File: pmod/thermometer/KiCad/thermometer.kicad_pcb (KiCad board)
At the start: 2 copper layers, 23 x 17 mm, 4 parts, among them J1 Conn_01x06_Pin, U1 DS18B20

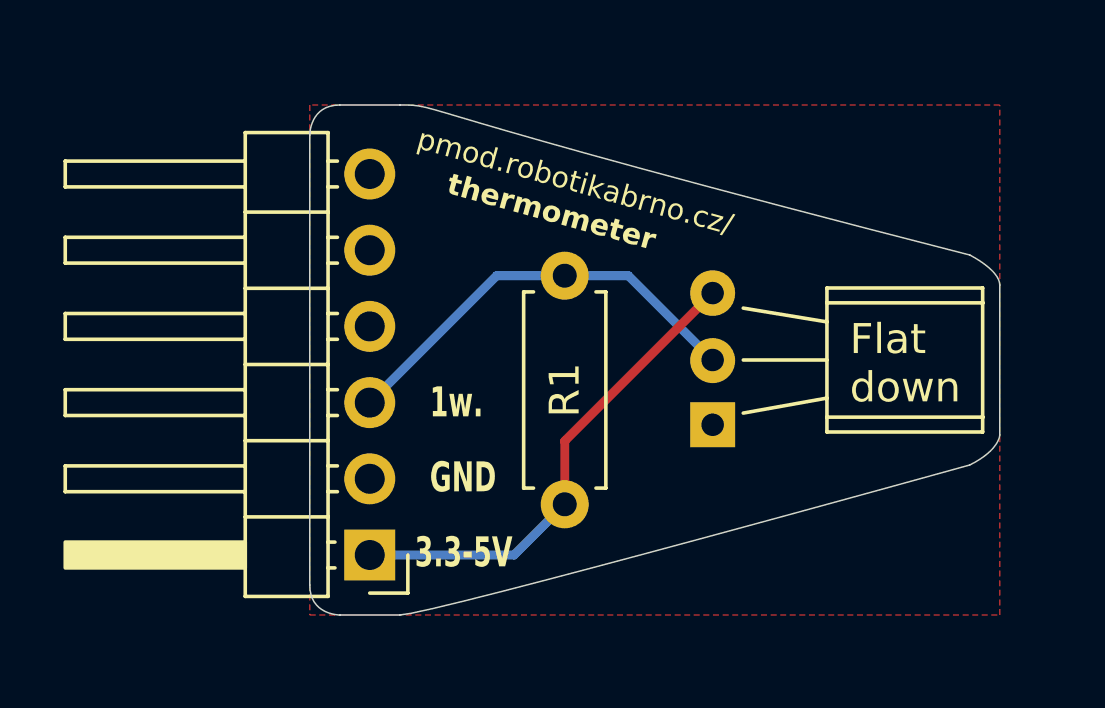
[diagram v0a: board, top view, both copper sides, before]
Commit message: add M3 mounting hole
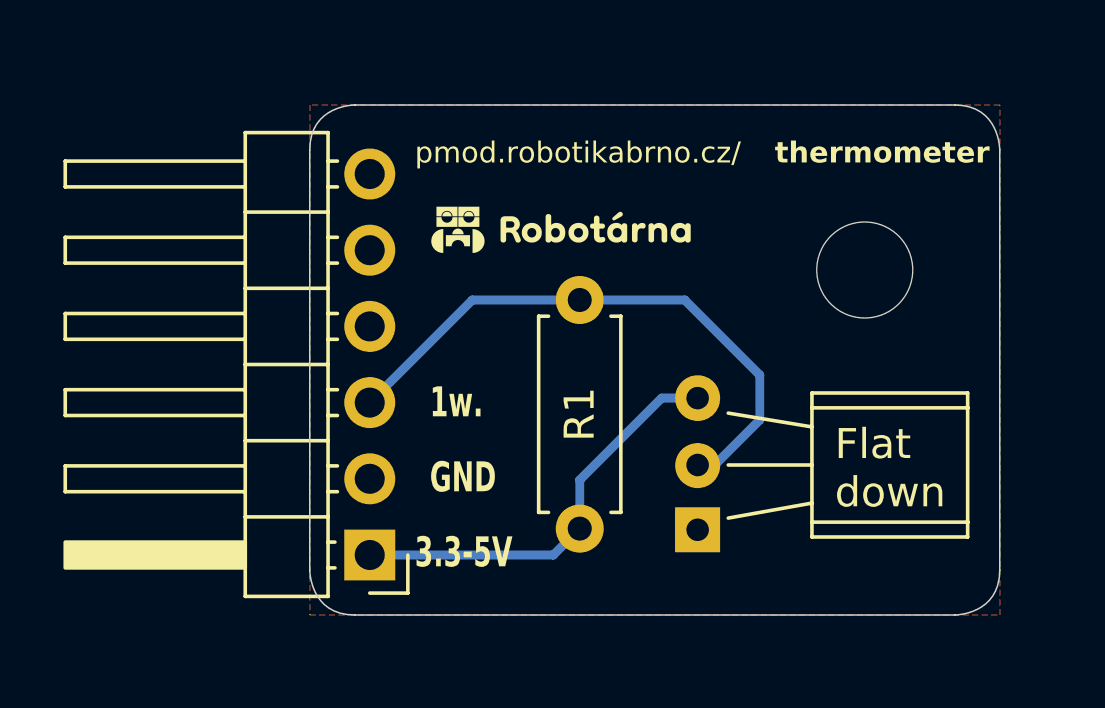
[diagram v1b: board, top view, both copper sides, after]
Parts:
- added H1: MountingHole, MountingHole:MountingHole_3.2mm_M3, F.Cu at (157.0, 107.0)
- moved G*** 10.1 mm to (166.5, 113.5)
- moved U1 3.54 mm to (151.4, 114.8)
- moved R1 0.95 mm to (147.5, 115.6)
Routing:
- net 1wire: track 14.3 -> 19.6 mm
- net VDD: track 16.3 -> 14.0 mm
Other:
- outline, holes or cut-outs redrawn

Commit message: fix: remove logo from the outside of the board
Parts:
- removed G***: LOGO, LOGO
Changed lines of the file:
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@@
 		)
-	)
-	(footprint "LOGO"
-		(layer "B.Cu")
-		(at 166.5 113.5 180)
-		(property "Reference" "G***"
-			(at 0 0 0)
-			(layer "B.SilkS")
-			(hide yes)
-			(effects
-				(font
-					(size 1.5 1.5)
-					(thickness 0.3)
-				)
-				(justify mirror)
-			)
-		)
-		(property "Value" "LOGO"
-			(at 0.75 0 0)
-			(layer "B.SilkS")
-			(hide yes)
-			(effects
-				(font
-					(size 1.5 1.5)
-					(thickness 0.3)
-				)
-				(justify mirror)
-			)
-		)
-		(property "Datasheet" ""
-			(at 0 0 0)
-			(layer "B.Fab")
-			(hide yes)
-			(effects
-				(font
-					(size 1.27 1.27)
-					(thickness 0.15)
-				)
-				(justify mirror)
-			)
-		)
-		(property "Description" ""
-			(at 0 0 0)
-			(layer "B.Fab")
-			(hide yes)
-			(effects
-				(font
-					(size 1.27 1.27)
-					(thickness 0.15)
-				)
-				(justify mirror)
-			)
-		)
-		(attr board_only exclude_from_pos_files exclude_from_bom)
-		(fp_poly
-			(pts
-				(xy -0.015495 0.107727) (xy 0.073096 0.094004) (xy 0.107377 0.084579) (xy 0.167235 0.060491) (xy 0.232458 0.026577)
-				(xy 0.294193 -0.012024) (xy 0.343586 -0.050172) (xy 0.350367 -0.056482) (xy 0.41717 -0.132255) (xy 0.473785 -0.218721)
-				(xy 0.51759 -0.310377) (xy 0.545964 -0.401719) (xy 0.556286 -0.487241) (xy 0.55629 -0.488887) (xy 0.55629 -0.53487)
-				(xy -0.093437 -0.530785) (xy -0.743164 -0.5267) (xy -0.737428 -0.485274) (xy -0.708842 -0.356527)
-				(xy -0.661064 -0.239758) (xy -0.595308 -0.136491) (xy -0.512788 -0.048247) (xy -0.414715 0.02345)
-				(xy -0.302304 0.07708) (xy -0.284064 0.083545) (xy -0.203295 0.102473) (xy -0.110699 0.110542)
-			)
-			(stroke
-				(width 0)
-				(type solid)
-			)
-			(fill yes)
-			(layer "B.SilkS")
-		)
-		(fp_poly
-			(pts
-				(xy -1.976608 1.369204) (xy -1.965572 1.278863) (xy -1.934261 1.186763) (xy -1.885373 1.096857)
-				(xy -1.821603 1.013102) (xy -1.745649 0.939455) (xy -1.660207 0.87987) (xy -1.633118 0.865324) (xy -1.521418 0.82163)
-				(xy -1.408192 0.799964) (xy -1.295813 0.799059) (xy -1.186659 0.817649) (xy -1.083104 0.854468)
-				(xy -0.987524 0.908251) (xy -0.902294 0.977732) (xy -0.829789 1.061644) (xy -0.772386 1.158721)
-				(xy -0.732459 1.267699) (xy -0.715687 1.354242) (xy -0.707432 1.420317) (xy -0.424732 1.420317)
-				(xy -0.142032 1.420317) (xy -0.142032 0.869945) (xy -0.142032 0.319572) (xy -1.343384 0.319572)
-				(xy -2.544735 0.319572) (xy -2.544735 0.869945) (xy -2.544735 1.420317) (xy -2.260672 1.420317)
-				(xy -1.976608 1.420317)
-			)
-			(stroke
-				(width 0)
-				(type solid)
-			)
-			(fill yes)
-			(layer "B.SilkS")
-		)
-		(fp_poly
-			(pts
-				(xy 2.367194 2.077214) (xy 2.367194 1.526841) (xy 2.084494 1.526841) (xy 1.801795 1.526841) (xy 1.793317 1.594696)
-				(xy 1.767405 1.711574) (xy 1.721406 1.818474) (xy 1.65749 1.913489) (xy 1.577823 1.99471) (xy 1.484573 2.06023)
-				(xy 1.379908 2.108143) (xy 1.265995 2.136541) (xy 1.169125 2.143927) (xy 1.083458 2.140655) (xy 1.010826 2.129079)
-				(xy 0.941377 2.106928) (xy 0.872191 2.07544) (xy 0.784569 2.020473) (xy 0.705796 1.949893) (xy 0.638582 1.867731)
-				(xy 0.585641 1.778014) (xy 0.549685 1.684773) (xy 0.533426 1.592037) (xy 0.532759 1.571226) (xy 0.532618 1.526841)
-				(xy 0.248555 1.526841) (xy -0.035509 1.526841) (xy -0.035509 2.077214) (xy -0.035509 2.627587) (xy 1.165843 2.627587)
-				(xy 2.367194 2.627587)
-			)
-			(stroke
-				(width 0)
-				(type solid)
-			)
-			(fill yes)
-			(layer "B.SilkS")
-		)
-		(fp_poly
-			(pts
-				(xy -0.142032 2.077214) (xy -0.142032 1.526841) (xy -0.424361 1.526841) (xy -0.70669 1.526841) (xy -0.720329 1.609428)
-				(xy -0.751546 1.731474) (xy -0.802438 1.840597) (xy -0.8724 1.935978) (xy -0.960828 2.016799) (xy -1.067116 2.082239)
-				(xy -1.070783 2.084059) (xy -1.185412 2.128069) (xy -1.302418 2.148697) (xy -1.420517 2.145949)
-				(xy -1.538428 2.119829) (xy -1.632635 2.081681) (xy -1.691155 2.046216) (xy -1.753557 1.997094)
-				(xy -1.813821 1.940094) (xy -1.865927 1.880997) (xy -1.903855 1.825582) (xy -1.908521 1.816822)
-				(xy -1.940805 1.74238) (xy -1.963964 1.667108) (xy -1.975657 1.599219) (xy -1.976608 1.577955) (xy -1.976608 1.526841)
-				(xy -2.260672 1.526841) (xy -2.544735 1.526841) (xy -2.544735 2.077214) (xy -2.544735 2.627587)
-				(xy -1.343384 2.627587) (xy -0.142032 2.627587)
-			)
-			(stroke
-				(width 0)
-				(type solid)
-			)
-			(fill yes)
-			(layer "B.SilkS")
-		)
-		(fp_poly
-			(pts
-				(xy 0.532618 1.37546) (xy 0.538683 1.316554) (xy 0.555063 1.247623) (xy 0.579039 1.178402) (xy 0.600862 1.131222)
-				(xy 0.638225 1.074613) (xy 0.690389 1.013585) (xy 0.750994 0.954332) (xy 0.813682 0.903047) (xy 0.872093 0.865926)
-				(xy 0.874417 0.86474) (xy 0.988866 0.819362) (xy 1.105773 0.797527) (xy 1.225282 0.799219) (xy 1.318699 0.816424)
-				(xy 1.411413 0.845806) (xy 1.489702 0.884609) (xy 1.561954 0.937629) (xy 1.611706 0.984042) (xy 1.690502 1.078888)
-				(xy 1.748159 1.18402) (xy 1.784214 1.298542) (xy 1.79006 1.330164) (xy 1.804404 1.420317) (xy 2.085799 1.420317)
-				(xy 2.367194 1.420317) (xy 2.367194 0.869945) (xy 2.367194 0.319572) (xy 1.165843 0.319572) (xy -0.035509 0.319572)
-				(xy -0.035509 0.869945) (xy -0.035509 1.420317) (xy 0.248555 1.420317) (xy 0.532618 1.420317)
-			)
-			(stroke
-				(width 0)
-				(type solid)
-			)
-			(fill yes)
-			(layer "B.SilkS")
-		)
-		(fp_poly
-			(pts
-				(xy 1.29012 -1.272367) (xy 1.29012 -1.905591) (xy 0.964631 -1.905591) (xy 0.639142 -1.905591) (xy 0.638936 -1.873042)
-				(xy 0.633218 -1.816134) (xy 0.618203 -1.747001) (xy 0.596193 -1.674055) (xy 0.569492 -1.605707)
-				(xy 0.560524 -1.586568) (xy 0.518551 -1.514742) (xy 0.463556 -1.446171) (xy 0.432788 -1.414029)
-				(xy 0.329759 -1.326283) (xy 0.218474 -1.259762) (xy 0.100908 -1.214811) (xy -0.020965 -1.191774)
-				(xy -0.145168 -1.190998) (xy -0.269727 -1.212828) (xy -0.392667 -1.25761) (xy -0.411048 -1.266428)
-				(xy -0.512144 -1.32763) (xy -0.602552 -1.404273) (xy -0.680009 -1.49302) (xy -0.742254 -1.590535)
-				(xy -0.787026 -1.693482) (xy -0.812061 -1.798525) (xy -0.816683 -1.864748) (xy -0.816683 -1.905591)
-				(xy -1.142172 -1.905591) (xy -1.467661 -1.905591) (xy -1.467661 -1.272367) (xy -1.467661 -0.639142)
-				(xy -0.08877 -0.639142) (xy 1.29012 -0.639142)
-			)
-			(stroke
-				(width 0)
-				(type solid)
-			)
-			(fill yes)
-			(layer "B.SilkS")
-		)
-		(fp_poly
-			(pts
-				(xy -1.775397 -1.301817) (xy -1.775397 -2.67493) (xy -1.8257 -2.673229) (xy -1.862595 -2.671293)
-				(xy -1.912767 -2.667785) (xy -1.96593 -2.66343) (xy -1.97069 -2.663005) (xy -2.095227 -2.64259)
-				(xy -2.226625 -2.604213) (xy -2.359196 -2.549981) (xy -2.487251 -2.482003) (xy -2.528416 -2.456349)
-				(xy -2.604188 -2.401102) (xy -2.685065 -2.331729) (xy -2.765128 -2.254093) (xy -2.83846 -2.174052)
-				(xy -2.899143 -2.097468) (xy -2.916919 -2.071618) (xy -3.00685 -1.913756) (xy -3.074512 -1.74959)
-				(xy -3.119593 -1.580467) (xy -3.141784 -1.407732) (xy -3.140771 -1.232731) (xy -3.131343 -1.143909)
-				(xy -3.094685 -0.962136) (xy -3.037378 -0.791803) (xy -2.959747 -0.63338) (xy -2.862121 -0.487339)
-				(xy -2.744827 -0.354151) (xy -2.608191 -0.234287) (xy -2.452541 -0.128218) (xy -2.407786 -0.102278)
-				(xy -2.330186 -0.062513) (xy -2.24923 -0.02898) (xy -2.160757 -0.00049) (xy -2.060609 0.024148)
-				(xy -1.944625 0.046122) (xy -1.8257 0.064266) (xy -1.775397 0.071296)
-			)
-			(stroke
-				(width 0)
-				(type solid)
-			)
-			(fill yes)
-			(layer "B.SilkS")
-		)
-		(fp_poly
-			(pts
-				(xy 1.627446 0.066346) (xy 1.655912 0.061888) (xy 1.699515 0.055606) (xy 1.749914 0.048695) (xy 1.761782 0.047116)
-				(xy 1.933665 0.012881) (xy 2.097011 -0.042335) (xy 2.250439 -0.116945) (xy 2.392566 -0.209367) (xy 2.522012 -0.318015)
-				(xy 2.637395 -0.441305) (xy 2.737334 -0.577652) (xy 2.820448 -0.725472) (xy 2.885354 -0.883181)
-				(xy 2.930673 -1.049193) (xy 2.955022 -1.221924) (xy 2.958993 -1.326164) (xy 2.947383 -1.501932)
-				(xy 2.913016 -1.672764) (xy 2.856588 -1.836938) (xy 2.778794 -1.992736) (xy 2.68033 -2.138438) (xy 2.58638 -2.247373)
-				(xy 2.45075 -2.373735) (xy 2.307077 -2.477838) (xy 2.15532 -2.559702) (xy 1.995435 -2.61935) (xy 1.827381 -2.656799)
-				(xy 1.714594 -2.669191) (xy 1.600532 -2.676938) (xy 1.592215 -2.436255) (xy 1.591045 -2.389) (xy 1.590009 -2.320183)
-				(xy 1.589115 -2.231913) (xy 1.58837 -2.126302) (xy 1.587779 -2.005459) (xy 1.58735 -1.871494) (xy 1.587089 -1.726516)
-				(xy 1.587003 -1.572636) (xy 1.587098 -1.411964) (xy 1.587381 -1.246608) (xy 1.587859 -1.07868) (xy 1.587918 -1.061528)
-				(xy 1.591938 0.072516)
-			)
-			(stroke
-				(width 0)
-				(type solid)
-			)
-			(fill yes)
-			(layer "B.SilkS")
-		)
-		(embedded_fonts no)
 	)
 	(gr_poly

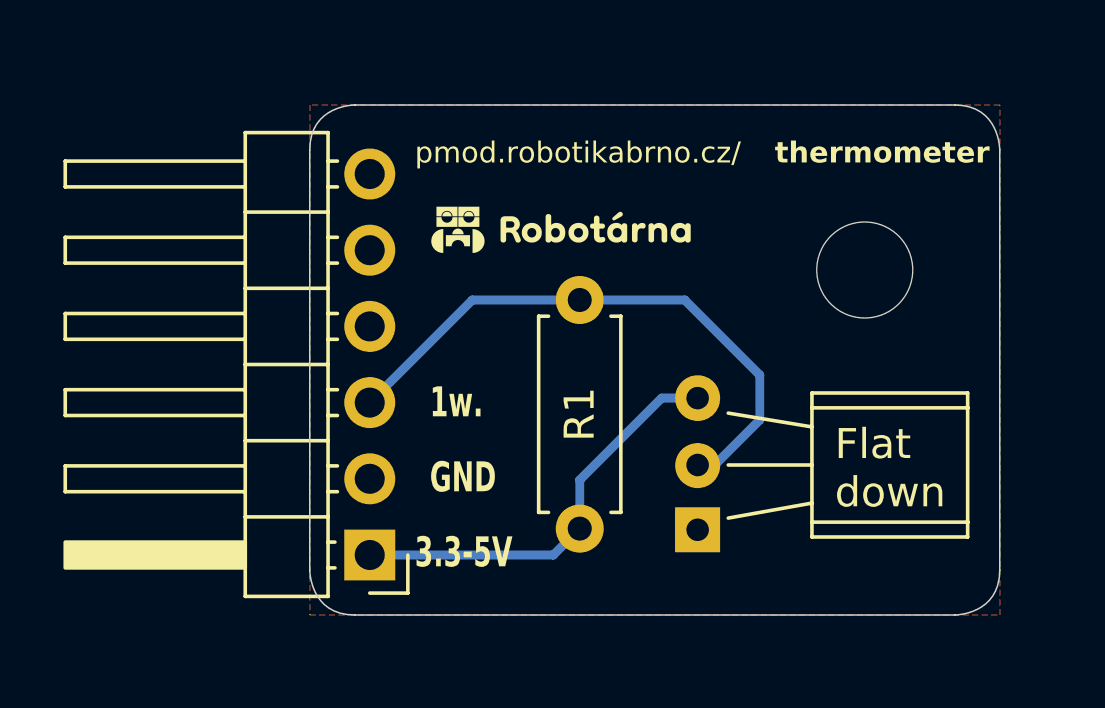
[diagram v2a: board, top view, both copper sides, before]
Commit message: enlarge text and add square logo
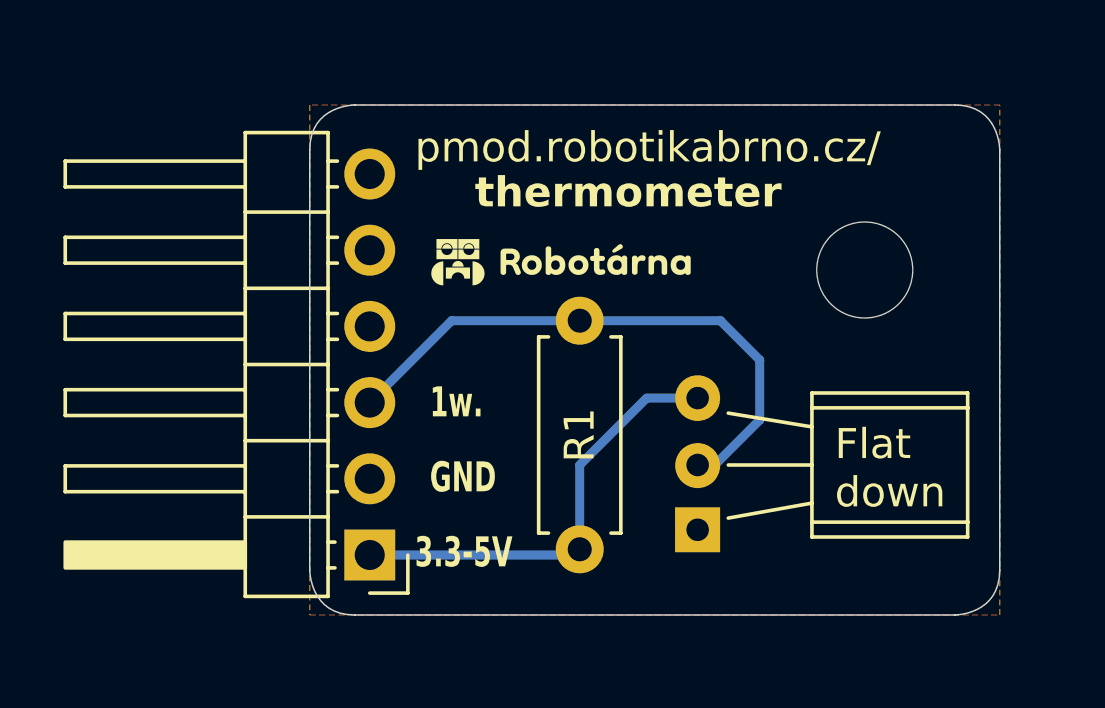
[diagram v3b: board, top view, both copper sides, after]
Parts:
- added G***: LOGO, LOGO, B.Cu at (157.0, 114.0)
- moved R1 0.69 mm to (147.5, 116.3)
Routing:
- net VDD: track 14.0 -> 14.7 mm

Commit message: minor fixes
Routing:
- net GND: vias 0 -> 8
- added copper zone on B.Cu, net GND
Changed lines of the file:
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@@
 			(psa4output no)
 			(plot_black_and_white yes)
+			(plotinvisibletext no)
 			(sketchpadsonfab no)
 			(plotpadnumbers no)
@@
 		(net 1)
 	)
+	(via
+		(at 142.6 105.4)
+		(size 0.6)
+		(drill 0.3)
+		(layers "F.Cu" "B.Cu")
+		(free yes)
+		(net 2)
+	)
+	(via
+		(at 152.2 106.6)
+		(size 0.6)
+		(drill 0.3)
+		(layers "F.Cu" "B.Cu")
+		(free yes)
+		(net 2)
+	)
+	(via
+		(at 154.4 117)
+		(size 0.6)
+		(drill 0.3)
+		(layers "F.Cu" "B.Cu")
+		(free yes)
+		(net 2)
+	)
+	(via
+		(at 148.2 103.6)
+		(size 0.6)
+		(drill 0.3)
+		(layers "F.Cu" "B.Cu")
+		(free yes)
+		(net 2)
+	)
+	(via
+		(at 147.6 111)
+		(size 0.6)
+		(drill 0.3)
+		(layers "F.Cu" "B.Cu")
+		(free yes)
+		(net 2)
+	)
+	(via
+		(at 158.6 112.6)
+		(size 0.6)
+		(drill 0.3)
+		(layers "F.Cu" "B.Cu")
+		(free yes)
+		(net 2)
+	)
+	(via
+		(at 144.2 112.8)
+		(size 0.6)
+		(drill 0.3)
+		(layers "F.Cu" "B.Cu")
+		(free yes)
+		(net 2)
+	)
+	(via
+		(at 159 117.2)
+		(size 0.6)
+		(drill 0.3)
+		(layers "F.Cu" "B.Cu")
+		(free yes)
+		(net 2)
+	)
 	(segment
 		(start 151.98 113.52)
@@
 		(net 2)
 		(net_name "GND")
-		(layer "F.Cu")
+		(layers "F.Cu" "B.Cu")
 		(hatch edge 0.5)
 		(connect_pads
-			(clearance 0.5)
+			(clearance 0.25)
 		)
 		(min_thickness 0.25)
 		(filled_areas_thickness no)
 		(fill yes
-			(thermal_gap 0.5)
+			(thermal_gap 0.25)
 			(thermal_bridge_width 0.5)
 		)
 		(polygon
 			(pts
-				(xy 138.5 101.5) (xy 138.5 118.5) (xy 161.5 118.5) (xy 161.5 101.5)
+				(xy 137.6 100) (xy 162.6 100.2) (xy 162.6 119.4) (xy 137.6 119.6)
 			)
 		)

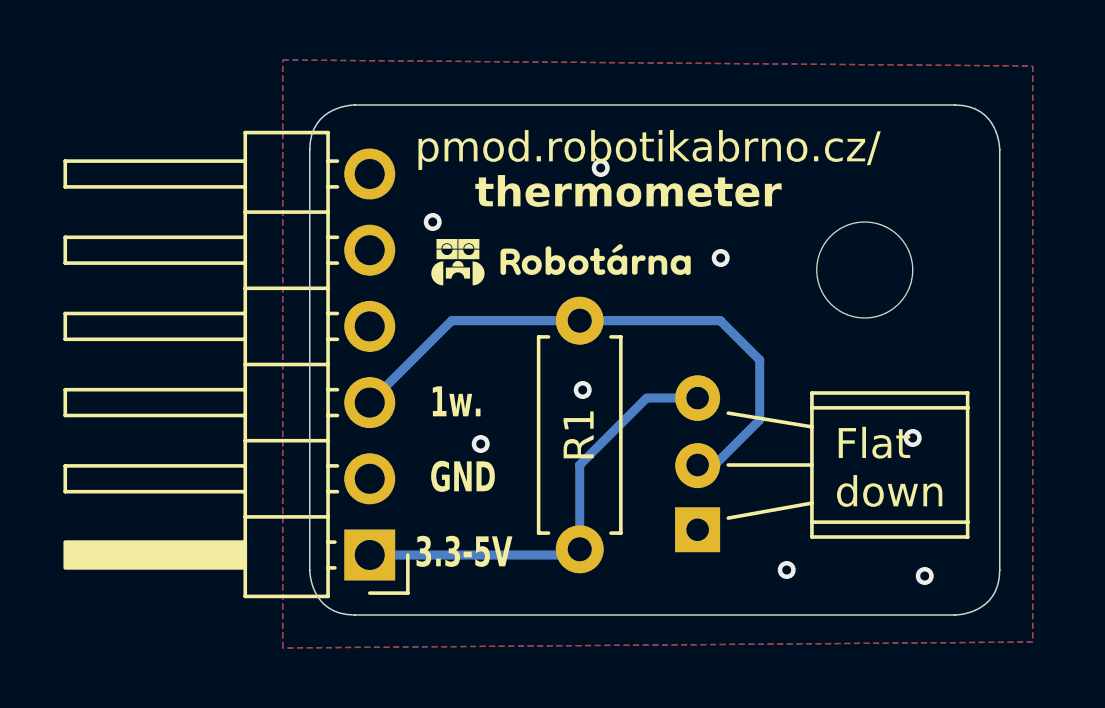
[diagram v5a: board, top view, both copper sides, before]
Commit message: fix: Pridal jsem opravy, ktere byly navrzene
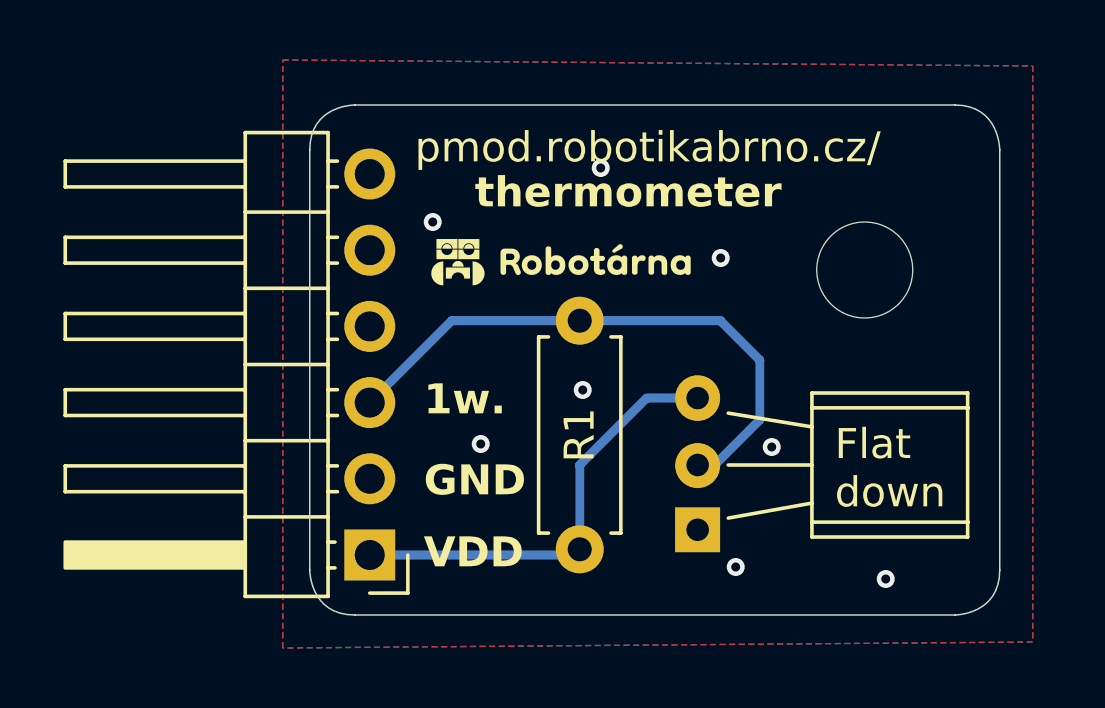
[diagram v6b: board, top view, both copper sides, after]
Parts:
- removed G***: LOGO, LOGO
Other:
- board text added: "VDD"
- board text removed: "3.3-5V"
